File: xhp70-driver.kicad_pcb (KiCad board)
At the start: 2 copper layers, 47.3 x 26.3 mm, 25 parts, among them J1 LEMO2, J2 AVR-ISP-6, Q1 Q_NMOS_GDS, U1 AL8871Q, U2 ATtiny85-20SU, U3 L7805

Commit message: Updates
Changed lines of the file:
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@@
   (page A4)
   (layers
-    (0 F.Cu signal hide)
-    (31 B.Cu signal hide)
+    (0 F.Cu signal)
+    (31 B.Cu signal)
     (32 B.Adhes user)
     (33 F.Adhes user)
@@
       (outputformat 1)
       (mirror false)
-      (drillshape 1)
+      (drillshape 0)
       (scaleselection 1)
-      (outputdirectory ""))
+      (outputdirectory "gerbers"))
   )
   (net 0 "")
@@
     (fp_line (start -3 1) (end -2.5 0.292893) (layer F.Fab) (width 0.1))
     (fp_line (start -2.5 0.292893) (end -2 1) (layer F.Fab) (width 0.1))
-    (pad MP smd roundrect (at 3.8 -1.2 270) (size 1.2 1.8) (layers F.Cu F.Paste F.Mask) (roundrect_rratio 0.208333))
-    (pad MP smd roundrect (at -3.8 -1.2 270) (size 1.2 1.8) (layers F.Cu F.Paste F.Mask) (roundrect_rratio 0.208333))
+    (pad MP smd roundrect (at 3.8 -1.2 270) (size 1.2 1.8) (layers F.Cu F.Paste F.Mask) (roundrect_rratio 0.2083325))
+    (pad MP smd roundrect (at -3.8 -1.2 270) (size 1.2 1.8) (layers F.Cu F.Paste F.Mask) (roundrect_rratio 0.2083325))
     (pad 6 smd roundrect (at 2.5 1.325 270) (size 0.6 1.55) (layers F.Cu F.Paste F.Mask) (roundrect_rratio 0.25)
       (net 1 GND))
@@
       (effects (font (size 1 1) (thickness 0.15)))
     )
-    (pad MP smd roundrect (at 1.8 -1.2 180) (size 1.2 1.8) (layers F.Cu F.Paste F.Mask) (roundrect_rratio 0.208333))
-    (pad MP smd roundrect (at -1.8 -1.2 180) (size 1.2 1.8) (layers F.Cu F.Paste F.Mask) (roundrect_rratio 0.208333))
+    (pad MP smd roundrect (at 1.8 -1.2 180) (size 1.2 1.8) (layers F.Cu F.Paste F.Mask) (roundrect_rratio 0.2083325))
+    (pad MP smd roundrect (at -1.8 -1.2 180) (size 1.2 1.8) (layers F.Cu F.Paste F.Mask) (roundrect_rratio 0.2083325))
     (pad 2 smd roundrect (at 0.5 1.325 180) (size 0.6 1.55) (layers F.Cu F.Paste F.Mask) (roundrect_rratio 0.25)
       (net 1 GND))
@@
       (effects (font (size 0.5 0.5) (thickness 0.08)))
     )
-    (pad 2 smd roundrect (at 0.9125 0 90) (size 1.025 1.4) (layers F.Cu F.Paste F.Mask) (roundrect_rratio 0.243902)
+    (pad 2 smd roundrect (at 0.9125 0 90) (size 1.025 1.4) (layers F.Cu F.Paste F.Mask) (roundrect_rratio 0.2439014634146341)
       (net 18 "Net-(R4-Pad2)"))
-    (pad 1 smd roundrect (at -0.9125 0 90) (size 1.025 1.4) (layers F.Cu F.Paste F.Mask) (roundrect_rratio 0.243902)
+    (pad 1 smd roundrect (at -0.9125 0 90) (size 1.025 1.4) (layers F.Cu F.Paste F.Mask) (roundrect_rratio 0.2439014634146341)
       (net 19 "Net-(R4-Pad1)"))
     (model ${KISYS3DMOD}/Resistor_SMD.3dshapes/R_0805_2012Metric.wrl
@@
       (effects (font (size 0.5 0.5) (thickness 0.08)))
     )
-    (pad 2 smd roundrect (at 0.9125 0) (size 1.025 1.4) (layers F.Cu F.Paste F.Mask) (roundrect_rratio 0.243902)
+    (pad 2 smd roundrect (at 0.9125 0) (size 1.025 1.4) (layers F.Cu F.Paste F.Mask) (roundrect_rratio 0.2439014634146341)
       (net 5 "Net-(R3-Pad2)"))
-    (pad 1 smd roundrect (at -0.9125 0) (size 1.025 1.4) (layers F.Cu F.Paste F.Mask) (roundrect_rratio 0.243902)
+    (pad 1 smd roundrect (at -0.9125 0) (size 1.025 1.4) (layers F.Cu F.Paste F.Mask) (roundrect_rratio 0.2439014634146341)
       (net 4 "Net-(Q1-Pad1)"))
     (model ${KISYS3DMOD}/Resistor_SMD.3dshapes/R_0805_2012Metric.wrl
@@
       (effects (font (size 1 1) (thickness 0.15)) (justify mirror))
     )
-    (pad 2 smd roundrect (at 2.9625 0 180) (size 1.225 3.35) (layers B.Cu B.Paste B.Mask) (roundrect_rratio 0.204082)
+    (pad 2 smd roundrect (at 2.9625 0 180) (size 1.225 3.35) (layers B.Cu B.Paste B.Mask) (roundrect_rratio 0.2040816326530612)
       (net 2 "Net-(C3-Pad2)"))
-    (pad 1 smd roundrect (at -2.9625 0 180) (size 1.225 3.35) (layers B.Cu B.Paste B.Mask) (roundrect_rratio 0.204082)
+    (pad 1 smd roundrect (at -2.9625 0 180) (size 1.225 3.35) (layers B.Cu B.Paste B.Mask) (roundrect_rratio 0.2040816326530612)
       (net 8 Batt+))
     (model ${KISYS3DMOD}/Resistor_SMD.3dshapes/R_2512_6332Metric.wrl
@@
       (effects (font (size 1 1) (thickness 0.15)))
     )
-    (pad 2 smd roundrect (at 2.9625 0 180) (size 1.225 3.35) (layers F.Cu F.Paste F.Mask) (roundrect_rratio 0.204082)
+    (pad 2 smd roundrect (at 2.9625 0 180) (size 1.225 3.35) (layers F.Cu F.Paste F.Mask) (roundrect_rratio 0.2040816326530612)
       (net 2 "Net-(C3-Pad2)"))
-    (pad 1 smd roundrect (at -2.9625 0 180) (size 1.225 3.35) (layers F.Cu F.Paste F.Mask) (roundrect_rratio 0.204082)
+    (pad 1 smd roundrect (at -2.9625 0 180) (size 1.225 3.35) (layers F.Cu F.Paste F.Mask) (roundrect_rratio 0.2040816326530612)
       (net 8 Batt+))
     (model ${KISYS3DMOD}/Resistor_SMD.3dshapes/R_2512_6332Metric.wrl
@@
       (effects (font (size 0.8 0.8) (thickness 0.12)))
     )
-    (pad 2 smd roundrect (at 1.5625 0) (size 1.325 1.8) (layers F.Cu F.Paste F.Mask) (roundrect_rratio 0.188679)
+    (pad 2 smd roundrect (at 1.5625 0) (size 1.325 1.8) (layers F.Cu F.Paste F.Mask) (roundrect_rratio 0.1886784905660377)
       (net 1 GND))
-    (pad 1 smd roundrect (at -1.5625 0) (size 1.325 1.8) (layers F.Cu F.Paste F.Mask) (roundrect_rratio 0.188679)
+    (pad 1 smd roundrect (at -1.5625 0) (size 1.325 1.8) (layers F.Cu F.Paste F.Mask) (roundrect_rratio 0.1886784905660377)
       (net 8 Batt+))
     (model ${KISYS3DMOD}/Capacitor_SMD.3dshapes/C_1206_3216Metric.wrl
@@
       (effects (font (size 0.8 0.8) (thickness 0.12)))
     )
-    (pad 2 smd roundrect (at 1.5625 0) (size 1.325 1.8) (layers F.Cu F.Paste F.Mask) (roundrect_rratio 0.188679)
+    (pad 2 smd roundrect (at 1.5625 0) (size 1.325 1.8) (layers F.Cu F.Paste F.Mask) (roundrect_rratio 0.1886784905660377)
       (net 2 "Net-(C3-Pad2)"))
-    (pad 1 smd roundrect (at -1.5625 0) (size 1.325 1.8) (layers F.Cu F.Paste F.Mask) (roundrect_rratio 0.188679)
+    (pad 1 smd roundrect (at -1.5625 0) (size 1.325 1.8) (layers F.Cu F.Paste F.Mask) (roundrect_rratio 0.1886784905660377)
       (net 16 "Net-(C3-Pad1)"))
     (model ${KISYS3DMOD}/Capacitor_SMD.3dshapes/C_1206_3216Metric.wrl
@@
       (effects (font (size 0.8 0.8) (thickness 0.12)))
     )
-    (pad 2 smd roundrect (at 1.5625 0) (size 1.325 1.8) (layers F.Cu F.Paste F.Mask) (roundrect_rratio 0.188679)
+    (pad 2 smd roundrect (at 1.5625 0) (size 1.325 1.8) (layers F.Cu F.Paste F.Mask) (roundrect_rratio 0.1886784905660377)
       (net 1 GND))
-    (pad 1 smd roundrect (at -1.5625 0) (size 1.325 1.8) (layers F.Cu F.Paste F.Mask) (roundrect_rratio 0.188679)
+    (pad 1 smd roundrect (at -1.5625 0) (size 1.325 1.8) (layers F.Cu F.Paste F.Mask) (roundrect_rratio 0.1886784905660377)
       (net 8 Batt+))
     (model ${KISYS3DMOD}/Capacitor_SMD.3dshapes/C_1206_3216Metric.wrl
@@
       (effects (font (size 0.8 0.8) (thickness 0.12)) (justify mirror))
     )
-    (pad 2 smd roundrect (at 1.5625 0) (size 1.325 1.8) (layers B.Cu B.Paste B.Mask) (roundrect_rratio 0.188679)
+    (pad 2 smd roundrect (at 1.5625 0) (size 1.325 1.8) (layers B.Cu B.Paste B.Mask) (roundrect_rratio 0.1886784905660377)
       (net 1 GND))
-    (pad 1 smd roundrect (at -1.5625 0) (size 1.325 1.8) (layers B.Cu B.Paste B.Mask) (roundrect_rratio 0.188679)
+    (pad 1 smd roundrect (at -1.5625 0) (size 1.325 1.8) (layers B.Cu B.Paste B.Mask) (roundrect_rratio 0.1886784905660377)
       (net 8 Batt+))
     (model ${KISYS3DMOD}/Capacitor_SMD.3dshapes/C_1206_3216Metric.wrl
@@
   )
   (zone (net 8) (net_name Batt+) (layer B.Cu) (hatch edge 0.508)
+    (priority 1)
     (connect_pads yes (clearance 0.508))
     (min_thickness 0.254)

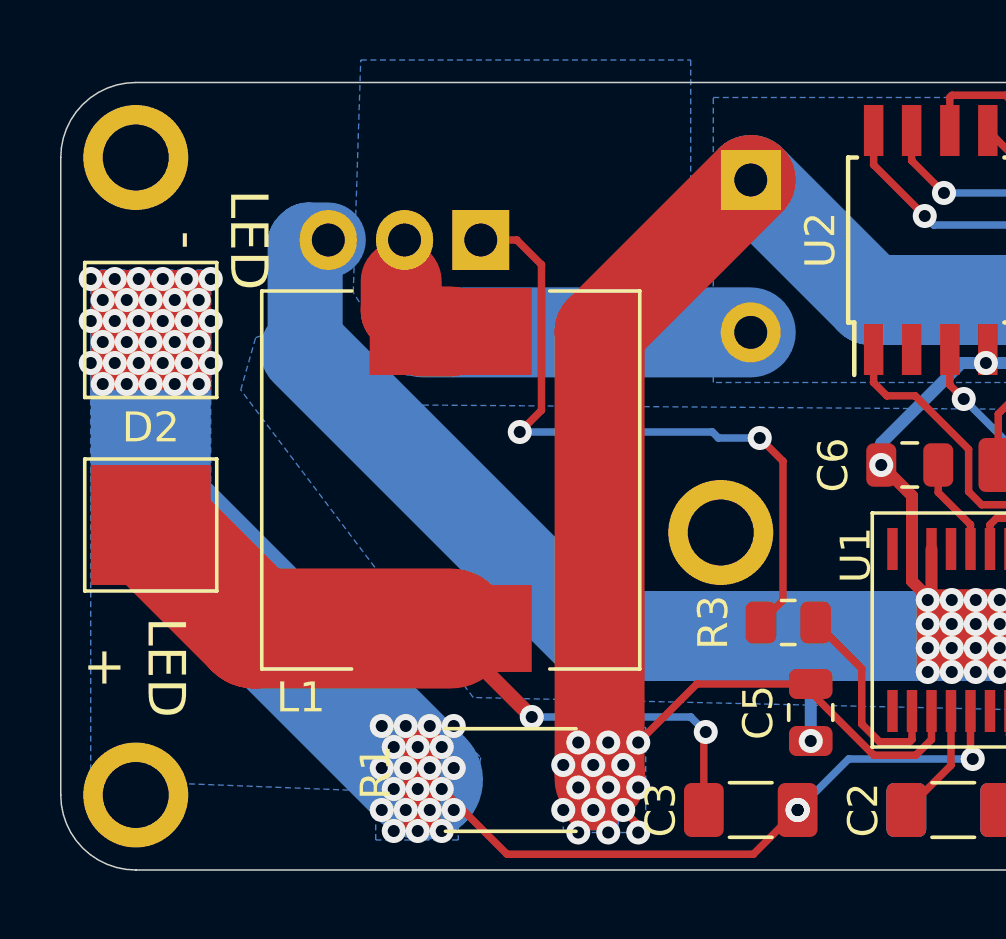
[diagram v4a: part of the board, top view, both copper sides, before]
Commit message: Tweak zone fills
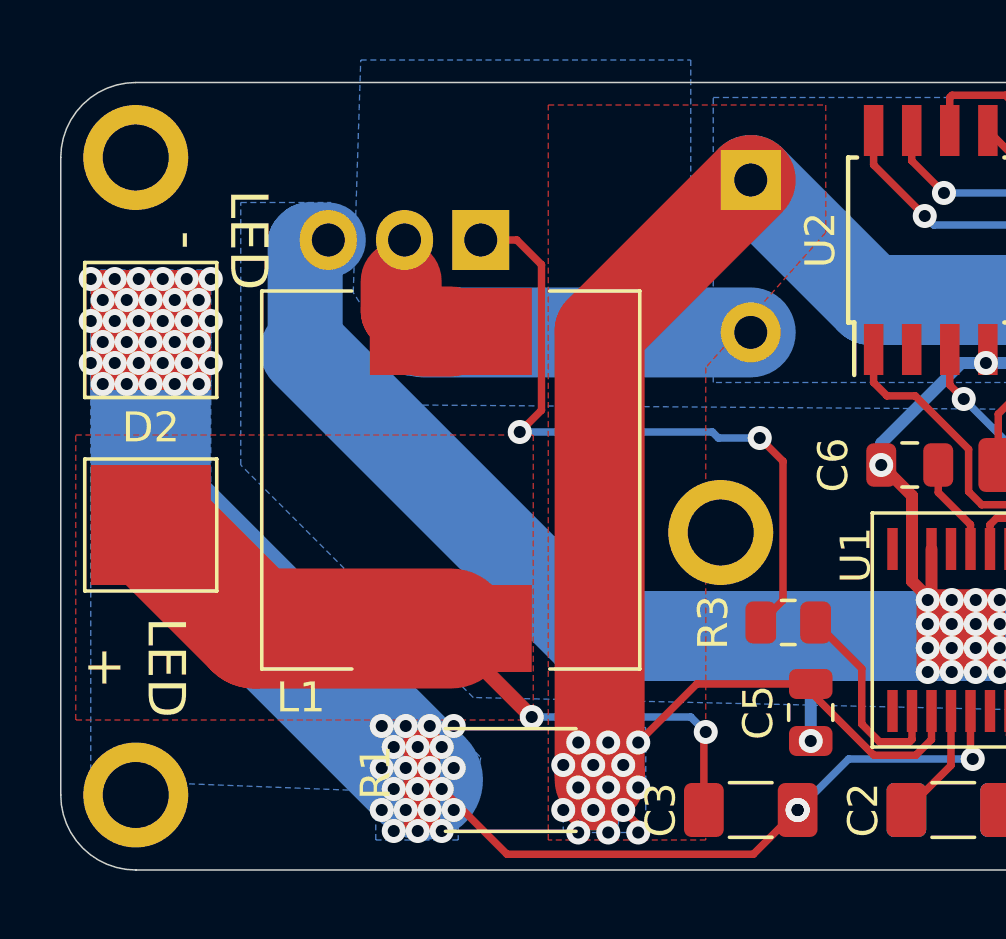
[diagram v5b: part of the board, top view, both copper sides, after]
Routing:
- added copper zone on F.Cu, net Batt+
- added copper zone on F.Cu, net Net-(C3-Pad1)
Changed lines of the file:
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@@
       (pts
         (xy 121.5 60.5) (xy 123.75 61.5) (xy 159 61.75) (xy 159 72) (xy 125.75 71.25)
-        (xy 118 61) (xy 118.5 59.25) (xy 121 58.5)
+        (xy 118 63.5) (xy 118 54.75) (xy 121 54.75)
       )
     )
@@
       )
     )
+  )
+  (zone (net 8) (net_name Batt+) (layer F.Cu) (hatch edge 0.508)
+    (priority 1)
+    (connect_pads yes (clearance 0.508))
+    (min_thickness 0.254)
+    (fill yes (arc_segments 32) (thermal_gap 0.508) (thermal_bridge_width 0.508))
+    (polygon
+      (pts
+        (xy 137.5 55.75) (xy 133.5 60.25) (xy 133.5 76) (xy 128.25 76) (xy 128.25 51.5)
+        (xy 137.5 51.5)
+      )
+    )
+  )
+  (zone (net 16) (net_name "Net-(C3-Pad1)") (layer F.Cu) (hatch edge 0.508)
+    (priority 1)
+    (connect_pads yes (clearance 0.508))
+    (min_thickness 0.254)
+    (fill yes (arc_segments 32) (thermal_gap 0.508) (thermal_bridge_width 0.508))
+    (polygon
+      (pts
+        (xy 127.75 72) (xy 112.5 72) (xy 112.5 62.5) (xy 127.75 62.5)
+      )
+    )

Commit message: Added name
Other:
- board text added: "intosite LED driver rev.1"
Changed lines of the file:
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@@
   (general
     (thickness 1.6)
-    (drawings 16)
+    (drawings 18)
     (tracks 313)
     (zones 0)
@@
   (page A4)
   (layers
-    (0 F.Cu signal)
-    (31 B.Cu signal)
-    (32 B.Adhes user)
-    (33 F.Adhes user)
-    (34 B.Paste user)
-    (35 F.Paste user)
+    (0 F.Cu signal hide)
+    (31 B.Cu signal hide)
+    (32 B.Adhes user hide)
+    (33 F.Adhes user hide)
+    (34 B.Paste user hide)
+    (35 F.Paste user hide)
     (36 B.SilkS user)
     (37 F.SilkS user)
-    (38 B.Mask user)
-    (39 F.Mask user)
-    (40 Dwgs.User user)
+    (38 B.Mask user hide)
+    (39 F.Mask user hide)
+    (40 Dwgs.User user hide)
     (41 Cmts.User user)
     (42 Eco1.User user)
@@
     (44 Edge.Cuts user)
     (45 Margin user)
-    (46 B.CrtYd user)
-    (47 F.CrtYd user)
-    (48 B.Fab user)
-    (49 F.Fab user)
+    (46 B.CrtYd user hide)
+    (47 F.CrtYd user hide)
+    (48 B.Fab user hide)
+    (49 F.Fab user hide)
   )
   (setup
@@
     (pad 1 thru_hole circle (at 0 0) (size 3.5 3.5) (drill 2.2) (layers *.Cu *.Mask))
   )
+  (gr_text "intosite\nLED driver rev.1" (at 153.75 71.5) (layer B.SilkS)
+    (effects (font (size 1.1 1.1) (thickness 0.275)) (justify left mirror))
+  )
+  (gr_text "intosite\nLED driver rev.1" (at 117.25 53) (layer F.SilkS)
+    (effects (font (size 1.1 1.1) (thickness 0.275)) (justify left))
+  )
   (gr_text "Batt\n-" (at 152.25 65.25 90) (layer B.SilkS)
     (effects (font (size 1.25 1.25) (thickness 0.3125)) (justify mirror))
@@
     (effects (font (size 1 1) (thickness 0.2)))
   )
-  (gr_text "LED\n-" (at 117.25 56 -90) (layer F.SilkS)
-    (effects (font (size 1.25 1.25) (thickness 0.3125)))
+  (gr_text "LED\n-" (at 117 55 -90) (layer F.SilkS)
+    (effects (font (size 1.25 1.25) (thickness 0.3125)) (justify left))
   )
   (gr_text "LED\n+ " (at 114.5 70.25 -90) (layer F.SilkS)

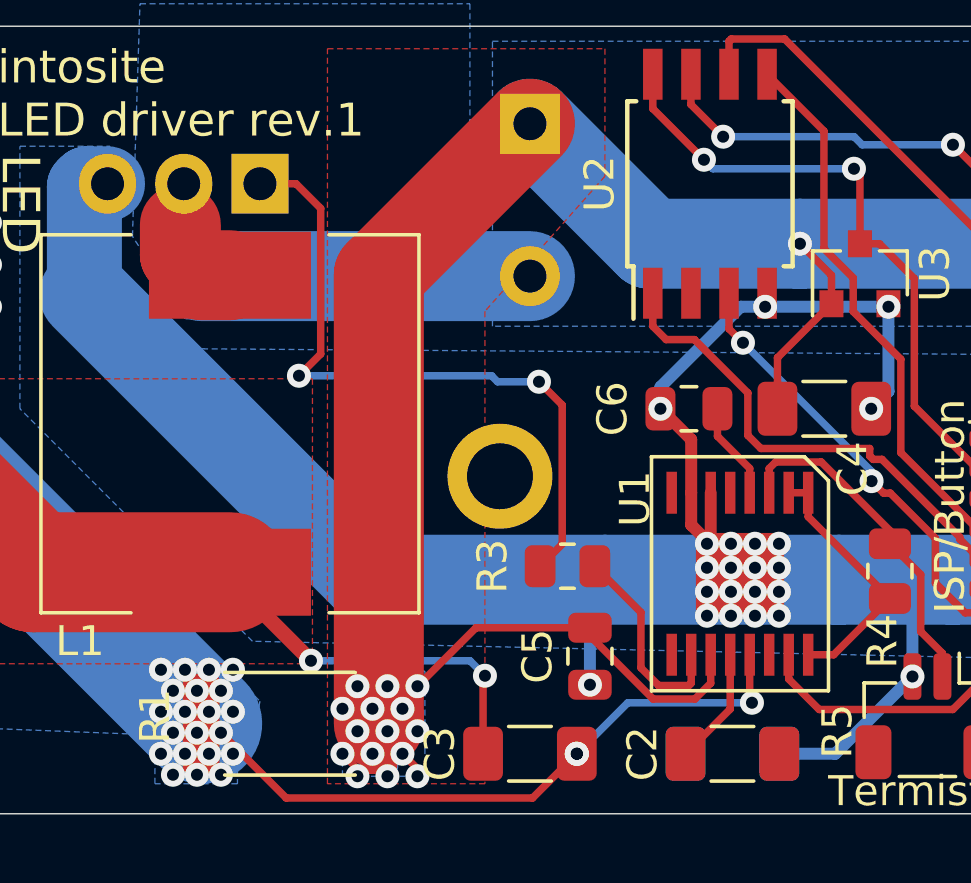
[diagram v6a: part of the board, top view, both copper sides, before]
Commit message: fixed unconnected tracks
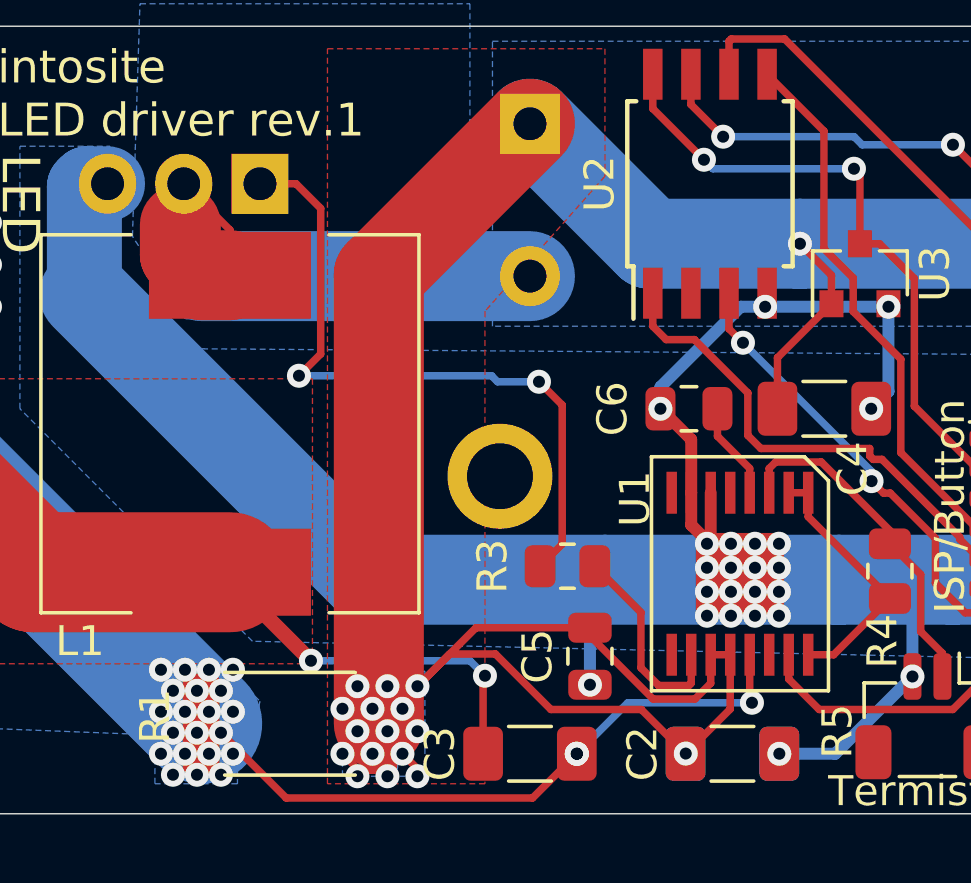
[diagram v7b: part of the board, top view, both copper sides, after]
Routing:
- net Batt+: track 70.1 -> 81.5 mm, vias 32 -> 33
- net Net-(D1-Pad2): track 16.1 -> 19.8 mm
- net GND: vias 39 -> 40

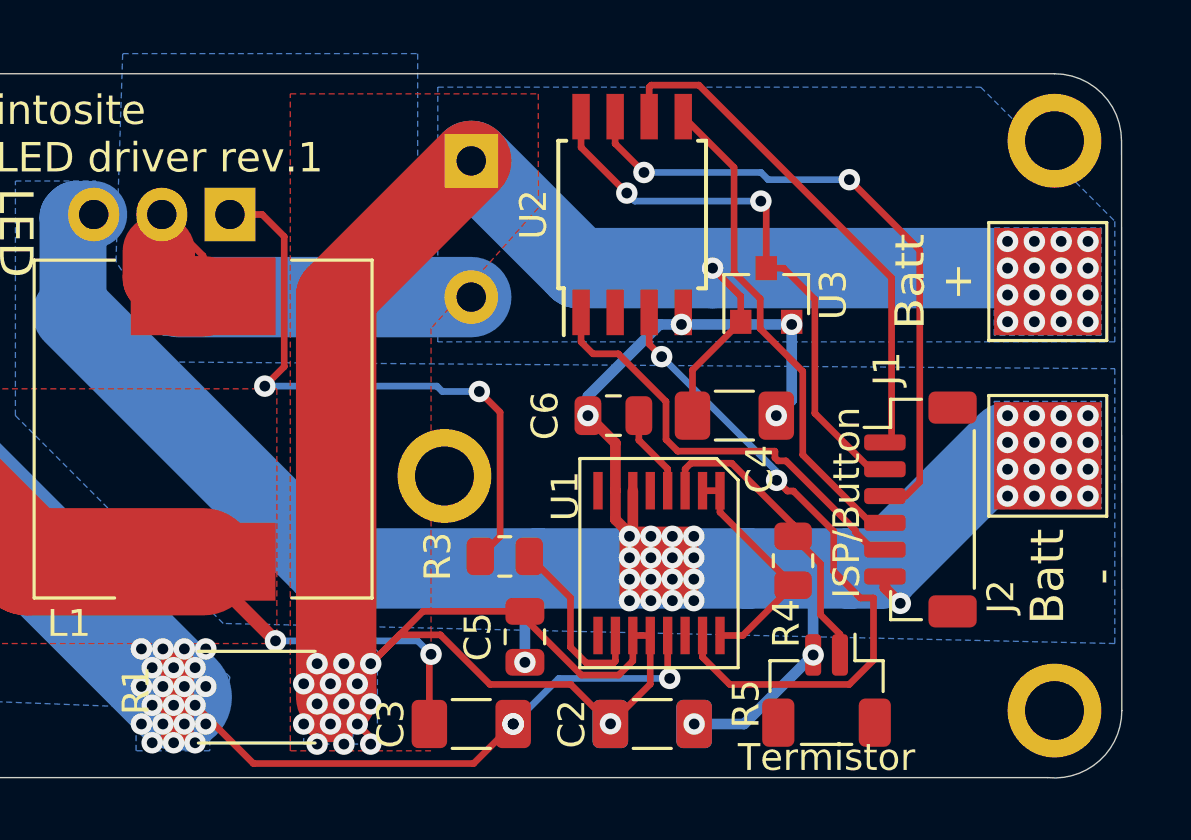
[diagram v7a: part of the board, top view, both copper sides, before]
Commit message: LED driver rev.1b - Added decoupling Capacitors for Attiny
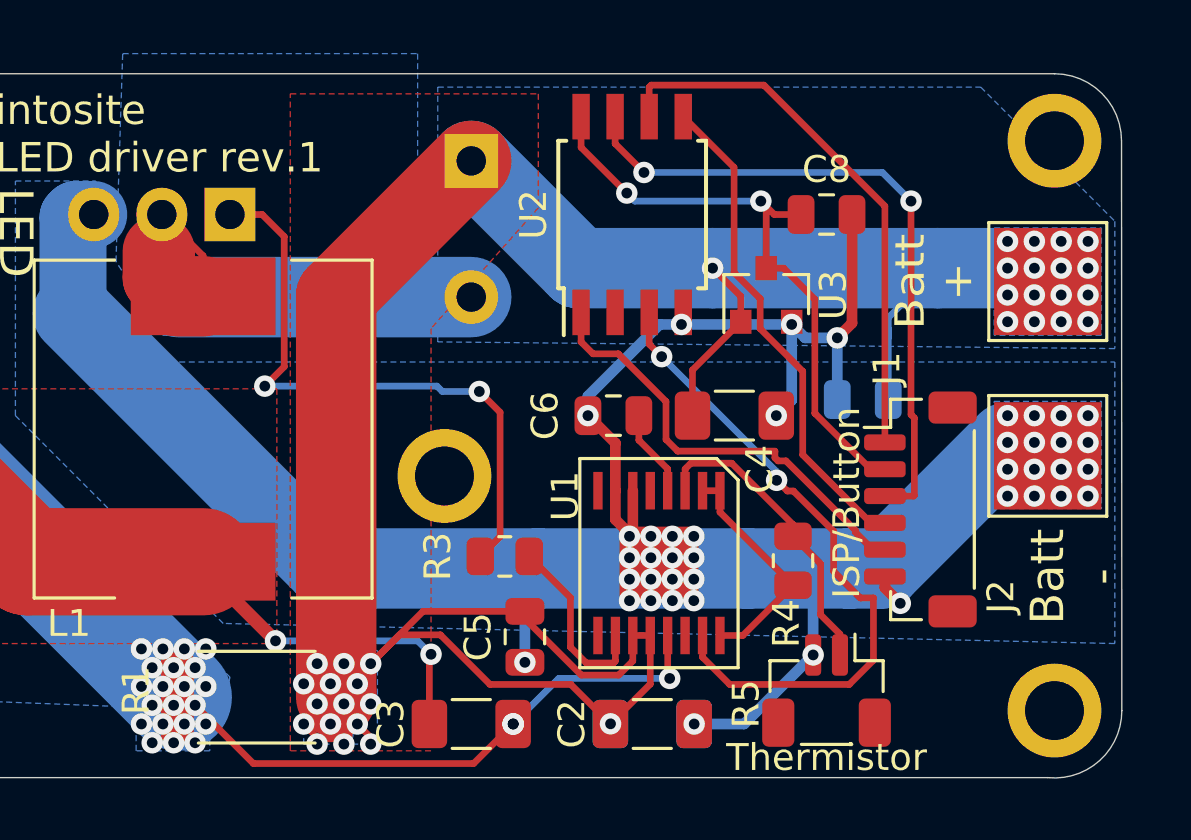
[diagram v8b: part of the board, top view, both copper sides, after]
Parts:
- added C7: 0.33uf, Capacitor_SMD:C_0805_2012Metric, B.Cu at (149.6, 62.9)
- added C8: 0.1uf, Capacitor_SMD:C_0805_2012Metric, F.Cu at (148.2, 56.0)
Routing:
- net GND: track 82.1 -> 91.2 mm, vias 40 -> 41
- net Batt+: track 81.5 -> 87.5 mm
- net Net-(C8-Pad1): track 21.5 -> 23.2 mm
- net Net-(J2-Pad3): track 24.2 -> 25.8 mm
- net Net-(J2-Pad1): track 19.3 -> 20.6 mm
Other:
- board text added: "Thermistor"
- board text added: "intosite LED driver rev.1b"
- board text removed: "Termistor"
